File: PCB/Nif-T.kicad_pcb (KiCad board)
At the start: 2 copper layers, 100 x 100 mm, 115 parts, among them J1 Barrel_Jack, J2 Conn_01x02, J3 Conn_02x03_Odd_Even, J4 Conn_02x03_Odd_Even, J5 Conn_02x03_Odd_Even, J6 Conn_02x03_Odd_Even, J7 Conn_02x03_Odd_Even, P1 USB_C_Plug, Q1 S8050, Q2 S8050, Q3 S8050, Q4 S8050, Q5 S8050, Q6 S8050, Q7 S8050, Q8 S8050, SW1 SW_Push, SW2 SW_Push, SW3 SW_Push, SW4 SW_SPDT, SW5 DSIC-05-LS-GER, SW6 DSIC-05-LS-GER, U1 ESP32-WROOM-32E(4MB), U10 DB128B-5.08-3P-BK-S, U11 DB128B-5.08-3P-BK-S, U2 LAN8720A-CP-TR, U3 DP1435-5V, U4 CH340C, U5 LM2596SX-5.0/NOPB, U6 AMS1117-3.3, U7 DB128B-5.08-3P-BK-S, U8 DB128B-5.08-3P-BK-S, U9 DB128B-5.08-3P-BK-S, X1 X322525MOB4SI

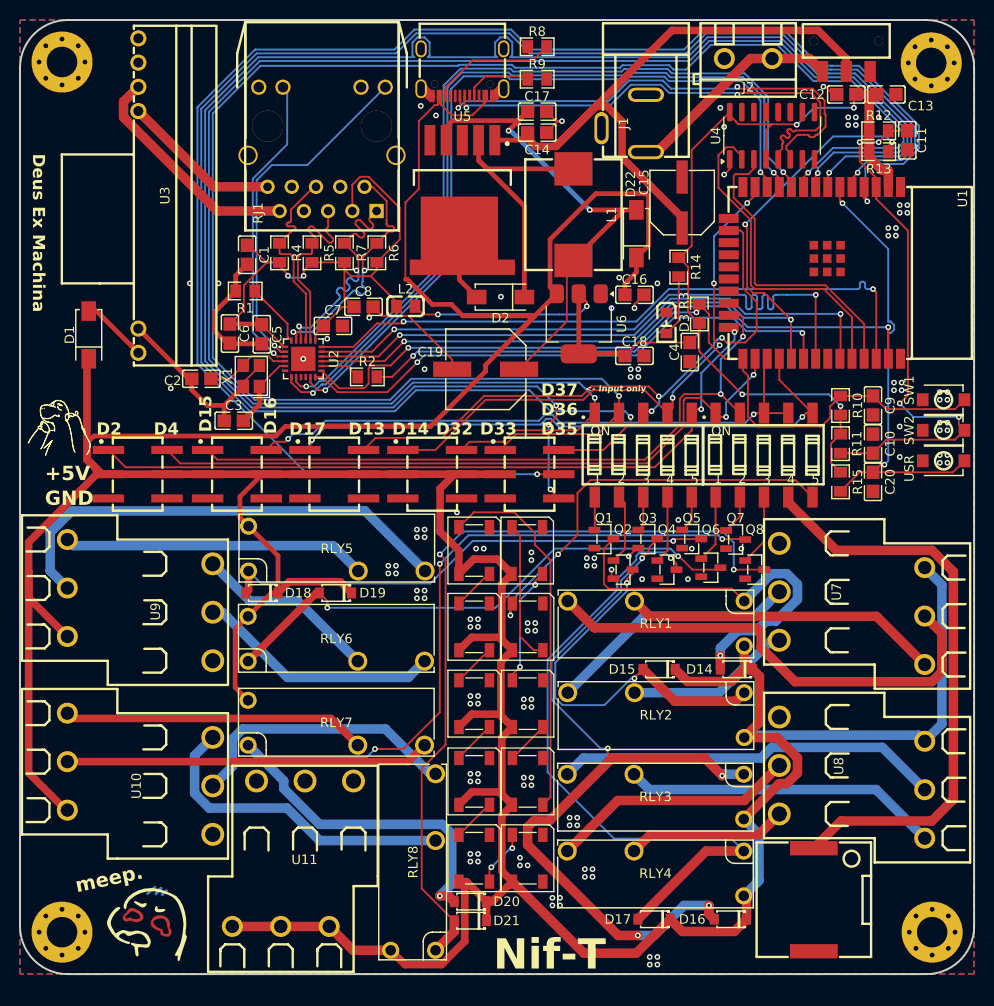
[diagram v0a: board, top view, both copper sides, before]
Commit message: Impedance matching and 4 layers
The PCB is now a 4 layer board for better ground pour coverage and to allow for proper impedance matching as needed by ethernet.
PCB Toolkit was used to calculate the new widths needed for proper ethernet trace impedance.
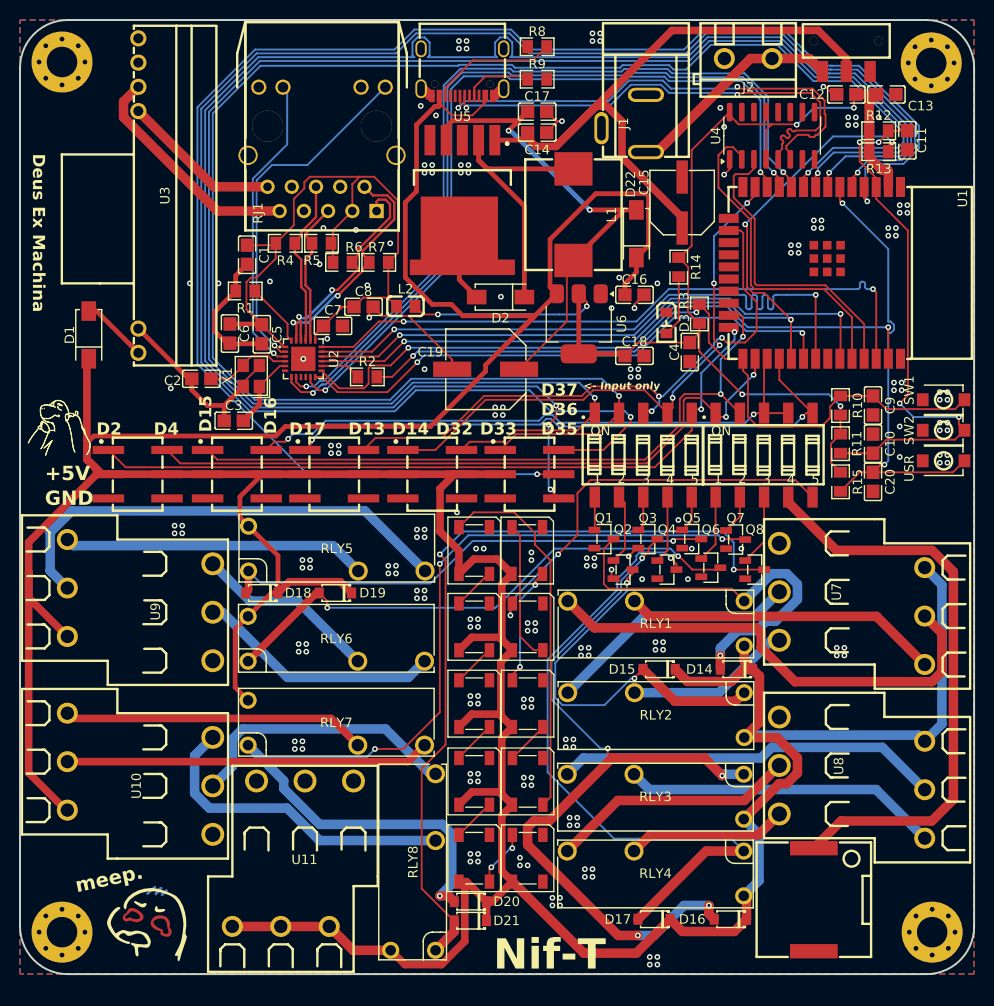
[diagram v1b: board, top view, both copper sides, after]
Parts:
- moved R5 1.41 mm to (181.6, 73.4), turned to 0 degrees
- moved R4 1.17 mm to (177.8, 73.4), turned to 180 degrees
- moved R6 1.02 mm to (187.6, 75.4), turned to 0 degrees
- moved R7 1.02 mm to (183.8, 75.4), turned to 180 degrees
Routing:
- net RX_CT: track 66.0 -> 73.2 mm, vias 2 -> 0
- net TX-: track 20.9 -> 15.3 mm
- net TX+: track 21.0 -> 17.5 mm
- net RX-: track 25.8 -> 22.6 mm
- net RX+: track 25.9 -> 24.6 mm
- net GND: vias 129 -> 199
- added copper zone on In1.Cu, net GND
- added copper zone on In2.Cu, net GND
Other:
- copper layers 2 -> 4
